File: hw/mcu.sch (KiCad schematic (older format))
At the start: 17 parts, among them U2 MSP430G2553IPW28

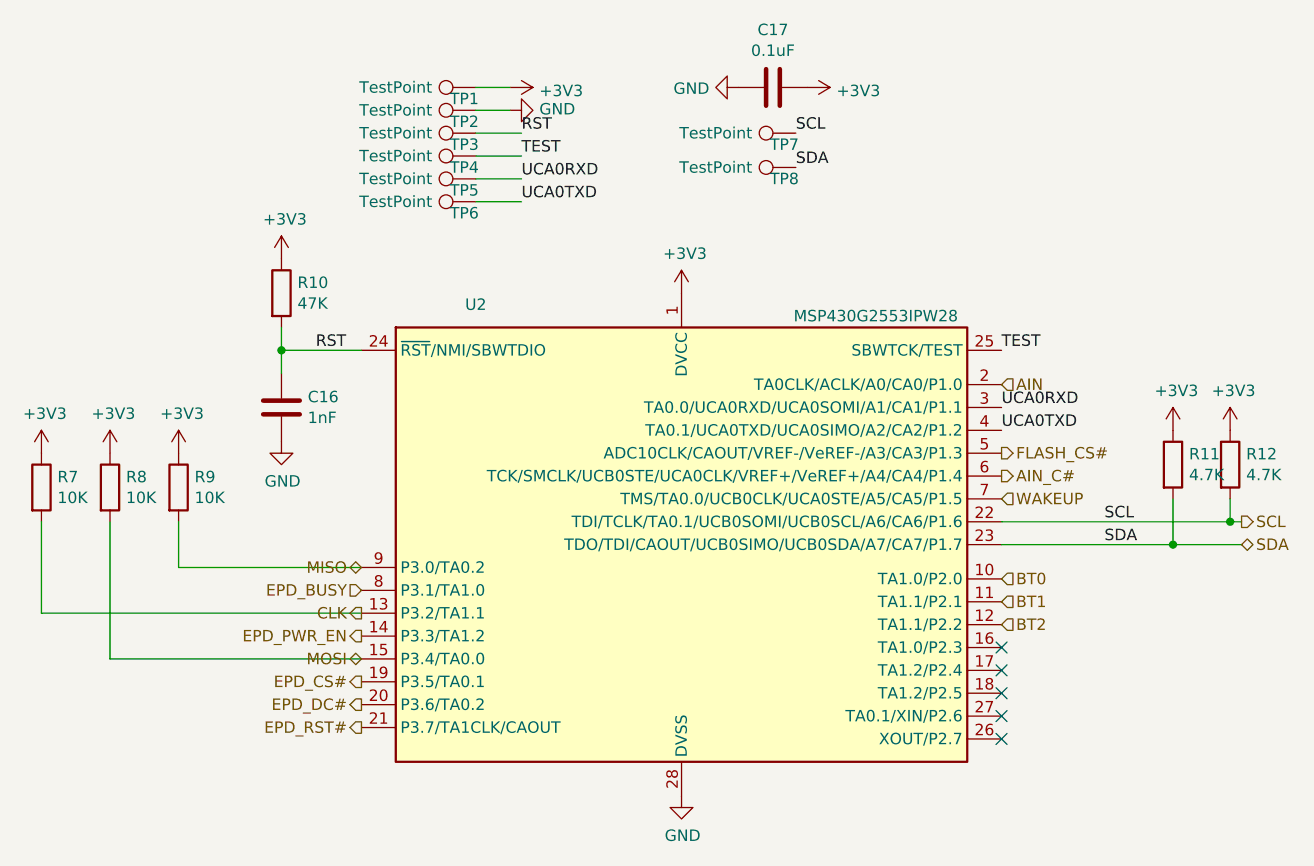
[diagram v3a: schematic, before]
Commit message: hw: 合并电源网络
取消墨水屏电源控制mos与独立电源域，墨水屏使用深度休眠模式，共用主
电源域。
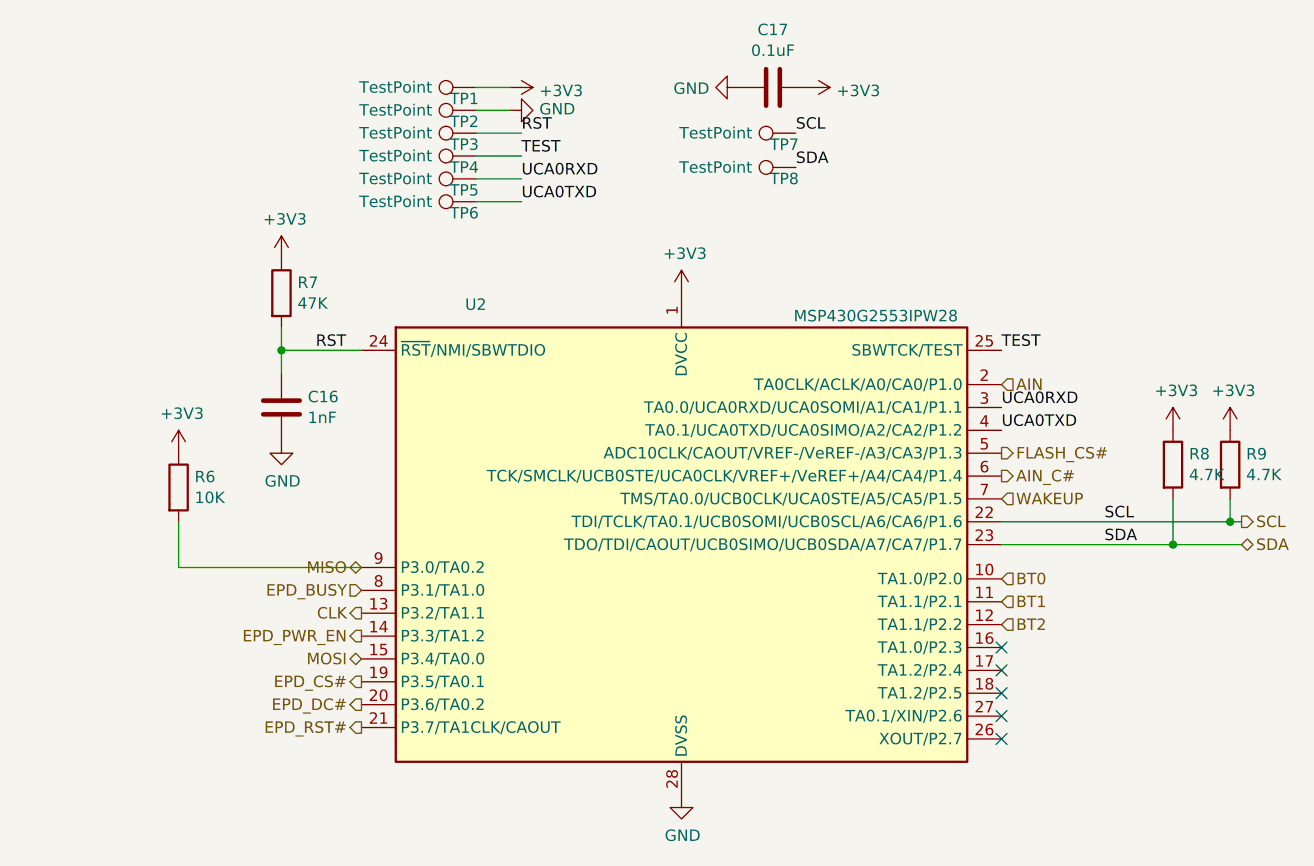
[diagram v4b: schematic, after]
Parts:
- removed R7, R8: 10K, Resistor_SMD:R_0603_1608Metric, symbol Device:R
- renumbered R9 to R6, R10 to R7, R11 to R8, R12 to R9
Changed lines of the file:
@@
 $EndDescr
 $Comp
-L power:+3V3 #PWR034
+L power:+3V3 #PWR032
 U 1 1 6113EAC6
 P 5900 2650
-F 0 "#PWR034" H 5900 2500 50  0001 C CNN
+F 0 "#PWR032" H 5900 2500 50  0001 C CNN
 F 1 "+3V3" H 5915 2823 50  0000 C CNN
 F 2 "" H 5900 2650 50  0001 C CNN
@@
 $EndComp
 $Comp
-L power:GND #PWR035
+L power:GND #PWR033
 U 1 1 6113F28C
 P 5900 4850
-F 0 "#PWR035" H 5900 4600 50  0001 C CNN
+F 0 "#PWR033" H 5900 4600 50  0001 C CNN
 F 1 "GND" H 5905 4677 50  0000 C CNN
 F 2 "" H 5900 4850 50  0001 C CNN
@@
 $EndComp
 $Comp
-L Device:R R10
+L Device:R R7
 U 1 1 6113FE92
 P 4150 2650
-F 0 "R10" H 4220 2696 50  0000 L CNN
+F 0 "R7" H 4220 2696 50  0000 L CNN
 F 1 "47K" H 4220 2605 50  0000 L CNN
 F 2 "Resistor_SMD:R_0603_1608Metric" V 4080 2650 50  0001 C CNN
@@
 	4150 2900 4150 3000
 $Comp
-L power:GND #PWR031
+L power:GND #PWR029
 U 1 1 61141837
 P 4150 3300
-F 0 "#PWR031" H 4150 3050 50  0001 C CNN
+F 0 "#PWR029" H 4150 3050 50  0001 C CNN
 F 1 "GND" H 4155 3127 50  0000 C CNN
 F 2 "" H 4150 3300 50  0001 C CNN
@@
 $EndComp
 $Comp
-L power:+3V3 #PWR030
+L power:+3V3 #PWR028
 U 1 1 61141D49
 P 4150 2500
-F 0 "#PWR030" H 4150 2350 50  0001 C CNN
+F 0 "#PWR028" H 4150 2350 50  0001 C CNN
 F 1 "+3V3" H 4165 2673 50  0000 C CNN
 F 2 "" H 4150 2500 50  0001 C CNN
@@
 $EndComp
 $Comp
-L power:+3V3 #PWR032
+L power:+3V3 #PWR030
 U 1 1 611466AB
 P 5150 1750
-F 0 "#PWR032" H 5150 1600 50  0001 C CNN
+F 0 "#PWR030" H 5150 1600 50  0001 C CNN
 F 1 "+3V3" V 5165 1878 50  0000 L CNN
 F 2 "" H 5150 1750 50  0001 C CNN
@@
 $EndComp
 $Comp
-L power:GND #PWR033
+L power:GND #PWR031
 U 1 1 61146C9B
 P 5150 1850
-F 0 "#PWR033" H 5150 1600 50  0001 C CNN
+F 0 "#PWR031" H 5150 1600 50  0001 C CNN
 F 1 "GND" V 5155 1722 50  0000 R CNN
 F 2 "" H 5150 1850 50  0001 C CNN
@@
 $EndComp
 $Comp
-L power:+3V3 #PWR037
+L power:+3V3 #PWR035
 U 1 1 610AD35D
 P 6450 1750
-F 0 "#PWR037" H 6450 1600 50  0001 C CNN
+F 0 "#PWR035" H 6450 1600 50  0001 C CNN
 F 1 "+3V3" V 6465 1878 50  0000 L CNN
 F 2 "" H 6450 1750 50  0001 C CNN
@@
 $EndComp
 $Comp
-L power:GND #PWR036
+L power:GND #PWR034
 U 1 1 610AD870
 P 6150 1750
-F 0 "#PWR036" H 6150 1500 50  0001 C CNN
+F 0 "#PWR034" H 6150 1500 50  0001 C CNN
 F 1 "GND" V 6155 1622 50  0000 R CNN
 F 2 "" H 6150 1750 50  0001 C CNN
@@
 NoConn ~ 7300 4200
 $Comp
-L Device:R R11
+L Device:R R8
 U 1 1 6117A5A3
 P 8050 3400
-F 0 "R11" H 8120 3446 50  0000 L CNN
+F 0 "R8" H 8120 3446 50  0000 L CNN
 F 1 "4.7K" H 8120 3355 50  0000 L CNN
 F 2 "Resistor_SMD:R_0603_1608Metric" V 7980 3400 50  0001 C CNN
@@
 $EndComp
 $Comp
-L Device:R R12
+L Device:R R9
 U 1 1 6117B220
 P 8300 3400
-F 0 "R12" H 8370 3446 50  0000 L CNN
+F 0 "R9" H 8370 3446 50  0000 L CNN
 F 1 "4.7K" H 8370 3355 50  0000 L CNN
 F 2 "Resistor_SMD:R_0603_1608Metric" V 8230 3400 50  0001 C CNN
@@
 	8300 3650 7300 3650
 $Comp
-L power:+3V3 #PWR038
+L power:+3V3 #PWR036
 U 1 1 6117E515
 P 8050 3250
-F 0 "#PWR038" H 8050 3100 50  0001 C CNN
+F 0 "#PWR036" H 8050 3100 50  0001 C CNN
 F 1 "+3V3" H 8065 3423 50  0000 C CNN
 F 2 "" H 8050 3250 50  0001 C CNN
@@
 $EndComp
 $Comp
-L power:+3V3 #PWR039
+L power:+3V3 #PWR037
 U 1 1 6117EB1C
 P 8300 3250
-F 0 "#PWR039" H 8300 3100 50  0001 C CNN
+F 0 "#PWR037" H 8300 3100 50  0001 C CNN
 F 1 "+3V3" H 8315 3423 50  0000 C CNN
 F 2 "" H 8300 3250 50  0001 C CNN
@@
 SCL
 $Comp
-L Device:R R9
+L Device:R R6
 U 1 1 611AD488
 P 3700 3500
-F 0 "R9" H 3770 3546 50  0000 L CNN
+F 0 "R6" H 3770 3546 50  0000 L CNN
 F 1 "10K" H 3770 3455 50  0000 L CNN
 F 2 "Resistor_SMD:R_0603_1608Metric" V 3630 3500 50  0001 C CNN
@@
 $EndComp
 $Comp
-L Device:R R8
-U 1 1 611B1822
-P 3400 3500
-F 0 "R8" H 3470 3546 50  0000 L CNN
-F 1 "10K" H 3470 3455 50  0000 L CNN
-F 2 "Resistor_SMD:R_0603_1608Metric" V 3330 3500 50  0001 C CNN
-F 3 "~" H 3400 3500 50  0001 C CNN
-	1    3400 3500
-	1    0    0    -1
-$EndComp
-$Comp
-L Device:R R7
-U 1 1 611B1D89
-P 3100 3500
-F 0 "R7" H 3170 3546 50  0000 L CNN
-F 1 "10K" H 3170 3455 50  0000 L CNN
-F 2 "Resistor_SMD:R_0603_1608Metric" V 3030 3500 50  0001 C CNN
-F 3 "~" H 3100 3500 50  0001 C CNN
-	1    3100 3500
-	1    0    0    -1
-$EndComp
-$Comp
 L power:+3V3 #PWR027
-U 1 1 611B222A
-P 3100 3350
-F 0 "#PWR027" H 3100 3200 50  0001 C CNN
-F 1 "+3V3" H 3115 3523 50  0000 C CNN
-F 2 "" H 3100 3350 50  0001 C CNN
-F 3 "" H 3100 3350 50  0001 C CNN
-	1    3100 3350
-	1    0    0    -1
-$EndComp
-$Comp
-L power:+3V3 #PWR028
-U 1 1 611B294F
-P 3400 3350
-F 0 "#PWR028" H 3400 3200 50  0001 C CNN
-F 1 "+3V3" H 3415 3523 50  0000 C CNN
-F 2 "" H 3400 3350 50  0001 C CNN
-F 3 "" H 3400 3350 50  0001 C CNN
-	1    3400 3350
-	1    0    0    -1
-$EndComp
-$Comp
-L power:+3V3 #PWR029
 U 1 1 611B2EF1
 P 3700 3350
-F 0 "#PWR029" H 3700 3200 50  0001 C CNN
+F 0 "#PWR027" H 3700 3200 50  0001 C CNN
 F 1 "+3V3" H 3715 3523 50  0000 C CNN
 F 2 "" H 3700 3350 50  0001 C CNN
@@
 Wire Wire Line
 	3700 3850 3700 3650
-Wire Wire Line
-	4500 4050 3100 4050
-Wire Wire Line
-	3100 4050 3100 3650
 Text HLabel 4500 4550 0    50   Output ~ 0
 EPD_RST#
 Text HLabel 4500 4050 0    50   Output ~ 0
 CLK
-Wire Wire Line
-	3400 4250 4500 4250
-Wire Wire Line
-	3400 3650 3400 4250
 $EndSCHEMATC
